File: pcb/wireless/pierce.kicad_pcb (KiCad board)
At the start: 2 copper layers, 112.2 x 91.4 mm, 27 parts, among them SW1 SW_PUSH, SW10 SW_PUSH, SW15 SW_PUSH, SW16 SW_PUSH, SW17 SW_PUSH, SW18 SW_PUSH, SW2 SW_PUSH, SW23 SW_PUSH, SW24 SW_PUSH, SW25 SW_PUSH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

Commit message: add reciever pcb for dual wireless setup
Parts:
- added Ref**: Val**, pierce:OSHW-LOGO-M, B.Cu at (77.8, 85.0)
- added Ref**: Val**, pierce:OSHW-LOGO-M, F.Cu at (77.8, 85.0)
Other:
- board text added: "by durken"
- board text added: "pierce 2.0"
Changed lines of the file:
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@@
   (general
     (thickness 1.6)
-    (drawings 148)
+    (drawings 152)
     (tracks 566)
     (zones 0)
-    (modules 27)
+    (modules 29)
     (nets 49)
   )
@@
     (add_net VCC)
   )
+  (module pierce:OSHW-LOGO-M (layer B.Cu)
+    (at 77.8256 85.0138 180)
+    (descr "OPEN-SOURCE HARDWARE (OSHW) LOGO - MEDIUM - SILKSCREEN")
+    (tags "OPEN-SOURCE HARDWARE (OSHW) LOGO - MEDIUM - SILKSCREEN")
+    (attr virtual)
+    (fp_text reference Ref** (at 0 0) (layer B.SilkS) hide
+      (effects (font (size 1.524 1.524) (thickness 0.15)) (justify mirror))
+    )
+    (fp_text value Val** (at 0 0) (layer B.SilkS) hide
+      (effects (font (size 1.524 1.524) (thickness 0.15)) (justify mirror))
+    )
+    (fp_poly (pts (xy 0.65532 -1.5875) (xy 0.90932 -1.45542) (xy 1.5367 -1.9685) (xy 1.9685 -1.5367)
+      (xy 1.45542 -0.90932) (xy 1.5875 -0.65532) (xy 1.67386 -0.38608) (xy 2.47904 -0.30226)
+      (xy 2.47904 0.30226) (xy 1.67386 0.38608) (xy 1.5875 0.65532) (xy 1.45542 0.90932)
+      (xy 1.9685 1.5367) (xy 1.5367 1.9685) (xy 0.90932 1.45542) (xy 0.65532 1.5875)
+      (xy 0.38608 1.67386) (xy 0.30226 2.47904) (xy -0.30226 2.47904) (xy -0.38608 1.67386)
+      (xy -0.65532 1.5875) (xy -0.90932 1.45542) (xy -1.5367 1.9685) (xy -1.9685 1.5367)
+      (xy -1.45542 0.90932) (xy -1.5875 0.65532) (xy -1.67386 0.38608) (xy -2.47904 0.30226)
+      (xy -2.47904 -0.30226) (xy -1.67386 -0.38608) (xy -1.5875 -0.65532) (xy -1.45542 -0.90932)
+      (xy -1.9685 -1.5367) (xy -1.5367 -1.9685) (xy -0.90932 -1.45542) (xy -0.65532 -1.5875)
+      (xy -0.29718 -0.72136) (xy -0.4318 -0.6477) (xy -0.55118 -0.55118) (xy -0.6477 -0.4318)
+      (xy -0.72136 -0.29718) (xy -0.76454 -0.1524) (xy -0.77978 0) (xy -0.76454 0.15748)
+      (xy -0.71374 0.31242) (xy -0.635 0.44958) (xy -0.53086 0.5715) (xy -0.40132 0.66802)
+      (xy -0.25654 0.7366) (xy -0.1016 0.77216) (xy 0.05588 0.77724) (xy 0.2159 0.7493)
+      (xy 0.36322 0.68834) (xy 0.49784 0.59944) (xy 0.6096 0.48514) (xy 0.69596 0.35052)
+      (xy 0.75438 0.20066) (xy 0.77978 0.04318) (xy 0.77216 -0.1143) (xy 0.73152 -0.26924)
+      (xy 0.6604 -0.41402) (xy 0.56134 -0.54102) (xy 0.43942 -0.64516) (xy 0.29718 -0.72136)) (layer B.SilkS) (width 0.01))
+  )
+  (module pierce:OSHW-LOGO-M (layer F.Cu)
+    (at 77.8256 85.0138)
+    (descr "OPEN-SOURCE HARDWARE (OSHW) LOGO - MEDIUM - SILKSCREEN")
+    (tags "OPEN-SOURCE HARDWARE (OSHW) LOGO - MEDIUM - SILKSCREEN")
+    (attr virtual)
+    (fp_text reference Ref** (at 0 0) (layer F.SilkS) hide
+      (effects (font (size 1.524 1.524) (thickness 0.15)))
+    )
+    (fp_text value Val** (at 0 0) (layer F.SilkS) hide
+      (effects (font (size 1.524 1.524) (thickness 0.15)))
+    )
+    (fp_poly (pts (xy 0.65532 1.5875) (xy 0.90932 1.45542) (xy 1.5367 1.9685) (xy 1.9685 1.5367)
+      (xy 1.45542 0.90932) (xy 1.5875 0.65532) (xy 1.67386 0.38608) (xy 2.47904 0.30226)
+      (xy 2.47904 -0.30226) (xy 1.67386 -0.38608) (xy 1.5875 -0.65532) (xy 1.45542 -0.90932)
+      (xy 1.9685 -1.5367) (xy 1.5367 -1.9685) (xy 0.90932 -1.45542) (xy 0.65532 -1.5875)
+      (xy 0.38608 -1.67386) (xy 0.30226 -2.47904) (xy -0.30226 -2.47904) (xy -0.38608 -1.67386)
+      (xy -0.65532 -1.5875) (xy -0.90932 -1.45542) (xy -1.5367 -1.9685) (xy -1.9685 -1.5367)
+      (xy -1.45542 -0.90932) (xy -1.5875 -0.65532) (xy -1.67386 -0.38608) (xy -2.47904 -0.30226)
+      (xy -2.47904 0.30226) (xy -1.67386 0.38608) (xy -1.5875 0.65532) (xy -1.45542 0.90932)
+      (xy -1.9685 1.5367) (xy -1.5367 1.9685) (xy -0.90932 1.45542) (xy -0.65532 1.5875)
+      (xy -0.29718 0.72136) (xy -0.4318 0.6477) (xy -0.55118 0.55118) (xy -0.6477 0.4318)
+      (xy -0.72136 0.29718) (xy -0.76454 0.1524) (xy -0.77978 0) (xy -0.76454 -0.15748)
+      (xy -0.71374 -0.31242) (xy -0.635 -0.44958) (xy -0.53086 -0.5715) (xy -0.40132 -0.66802)
+      (xy -0.25654 -0.7366) (xy -0.1016 -0.77216) (xy 0.05588 -0.77724) (xy 0.2159 -0.7493)
+      (xy 0.36322 -0.68834) (xy 0.49784 -0.59944) (xy 0.6096 -0.48514) (xy 0.69596 -0.35052)
+      (xy 0.75438 -0.20066) (xy 0.77978 -0.04318) (xy 0.77216 0.1143) (xy 0.73152 0.26924)
+      (xy 0.6604 0.41402) (xy 0.56134 0.54102) (xy 0.43942 0.64516) (xy 0.29718 0.72136)) (layer F.SilkS) (width 0.01))
+  )
   (module pierce:MX_ALPS_PG1350_noLed (layer F.Cu)
     (at 79.628391 51.955144)
@@
       (net 21 VCC))
   )
+  (gr_text "pierce 2.0" (at 69.342 83.6168) (layer B.SilkS)
+    (effects (font (size 1.5 1.5) (thickness 0.3)) (justify mirror))
+  )
+  (gr_text "by durken" (at 69.342 86.3092) (layer F.SilkS)
+    (effects (font (size 1.5 1.5) (thickness 0.3) italic))
+  )
+  (gr_text "by durken" (at 69.469 86.2584) (layer B.SilkS)
+    (effects (font (size 1.5 1.5) (thickness 0.3) italic) (justify mirror))
+  )
+  (gr_text "pierce 2.0" (at 69.342 83.6168) (layer F.SilkS)
+    (effects (font (size 1.5 1.5) (thickness 0.3)))
+  )
   (gr_text CLK (at 56.9722 82.1436) (layer F.SilkS)

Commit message: small adjustments
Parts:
- moved Ref** 0.38 mm to (78.2, 85.0) (x2)
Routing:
- net VCC: track 165.1 -> 167.6 mm
- net SW32L: track 73.8 -> 75.4 mm

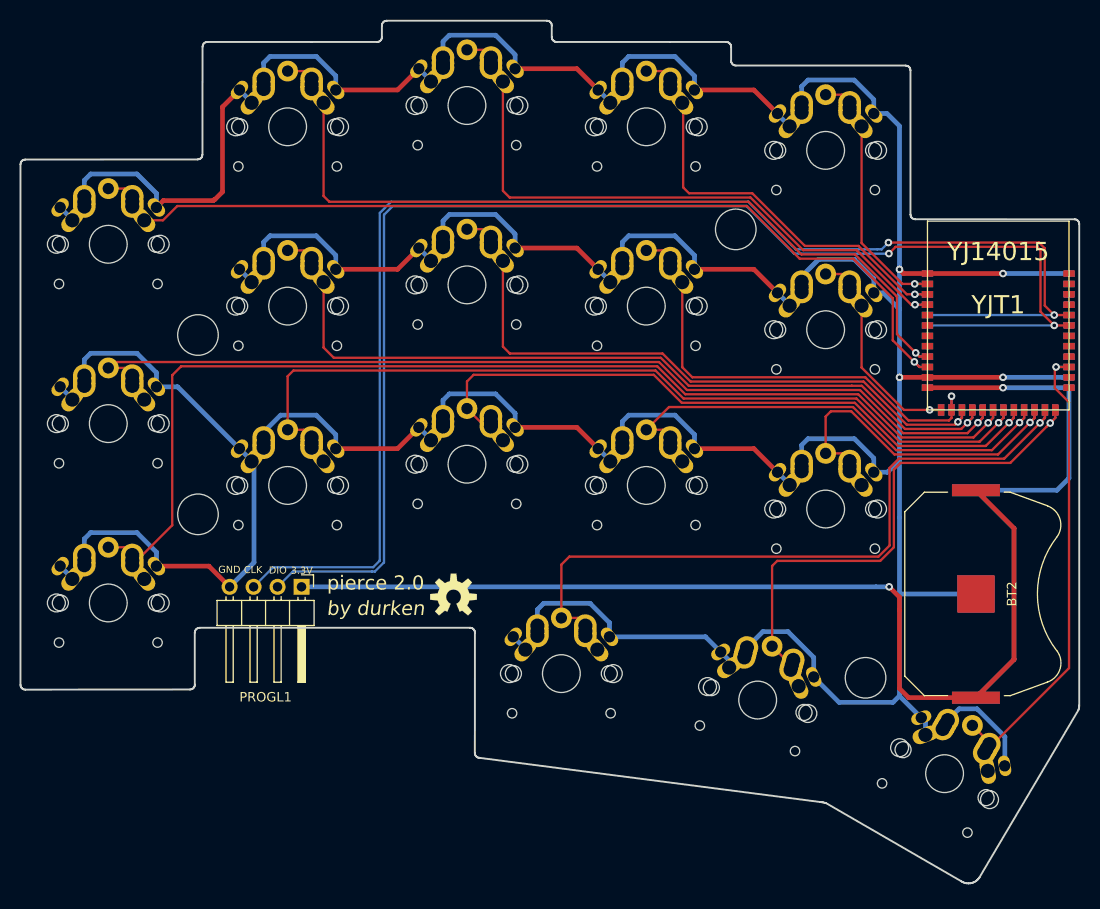
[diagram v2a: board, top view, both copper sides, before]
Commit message: add gnd planes
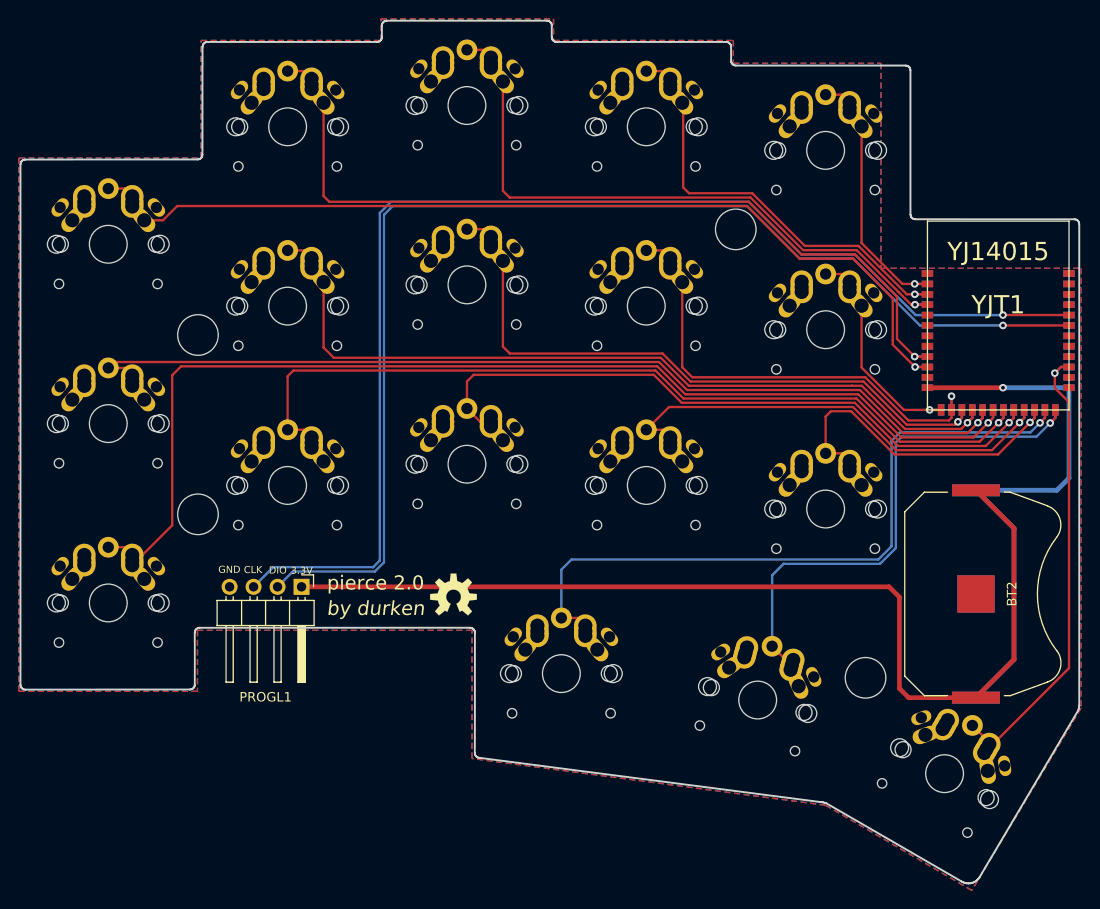
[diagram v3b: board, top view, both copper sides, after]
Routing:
- net GND: track 566.4 -> 0.33 mm, vias 4 -> 0
- net DIOL: track 145.2 -> 127.2 mm, vias 2 -> 1
- net CLKL: track 147.4 -> 129.6 mm, vias 2 -> 1
- net SW32L: track 75.4 -> 76.9 mm
- net SW33L: track 57.6 -> 58.8 mm
- net VCC: vias 2 -> 1
- added copper zone on B.Cu, net GND
- added copper zone on F.Cu, net GND

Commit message: small visual adjustments
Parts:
- removed the Ref** at (78.2, 85.0) (x2)
- added REF**: OSHW-Logo2_7.3x6mm_SilkScreen, pierce:OSHW-Logo2_7.3x6mm_SilkScreen, B.Cu at (79.3, 84.8)
- added REF**: OSHW-Logo2_7.3x6mm_SilkScreen, pierce:OSHW-Logo2_7.3x6mm_SilkScreen, F.Cu at (79.3, 84.8)
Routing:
- net GND: track 0.33 -> 2.46 mm, vias 0 -> 1
- net SW34L: track 53.6 -> 55.2 mm
- net VCC: vias 1 -> 3
